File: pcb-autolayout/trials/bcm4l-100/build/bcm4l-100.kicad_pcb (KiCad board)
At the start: 4 copper layers, 80 x 60 mm, 120 parts, among them J1 MicroFit 2x4, J2 MicroFit 2x6, J3 SWD, Q1 SQD40P06 (P-MOS), Q11 AO3401A, Q12 MMBT3904, Q13 AO3401A, Q14 MMBT3904, Q15 AO3401A, Q16 MMBT3904, Q17 AO3401A, Q18 MMBT3904, SW1 RESET, U1 TPS54202, U2 AMS1117-3.3, U3 TJA1051T/3, U4 TJA1021T/20, U5 STM32F103C8T6, Y1 8MHz

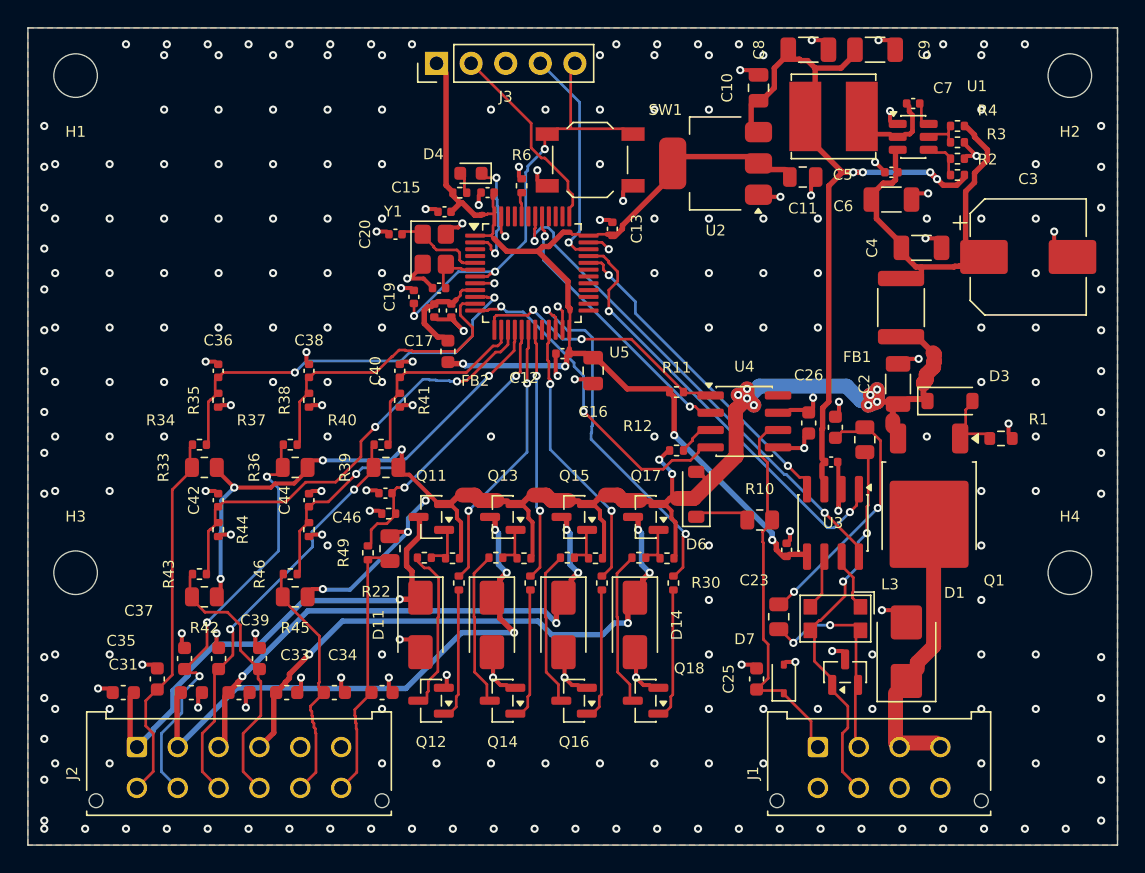
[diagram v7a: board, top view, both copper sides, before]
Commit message: 16/16 rule không chỉnh tay; placement repair; tất định KiCad 9 thật sự
- placer.repair_near: gỡ-đặt lại quanh chân đích, điểm từ điển (vượt C, vượt M)
- NEAR_REACH: linh kiện near vươn khỏi vùng khối tới quanh chân đích
- checks.near_gap: thước đo near dùng chung checker/placer
- kicad_board: canonicalize trước khi tô zone (KiCad 9 tô lệch µm theo thứ tự UUID);
  chuẩn hoá đa giác tô (bỏ đỉnh thẳng hàng, xoay, sắp)
- tests/test_placer.py; trial 16/16 KiCad 9 f116fcd59dba83db, KiCad 7 33b4f9200f4283d2

Co-Authored-By: Claude Opus 5.5 <noreply@anthropic.com>
Claude-Session: https://claude.ai/code/session_012jwodCpQFB8wopi3P3TnUz
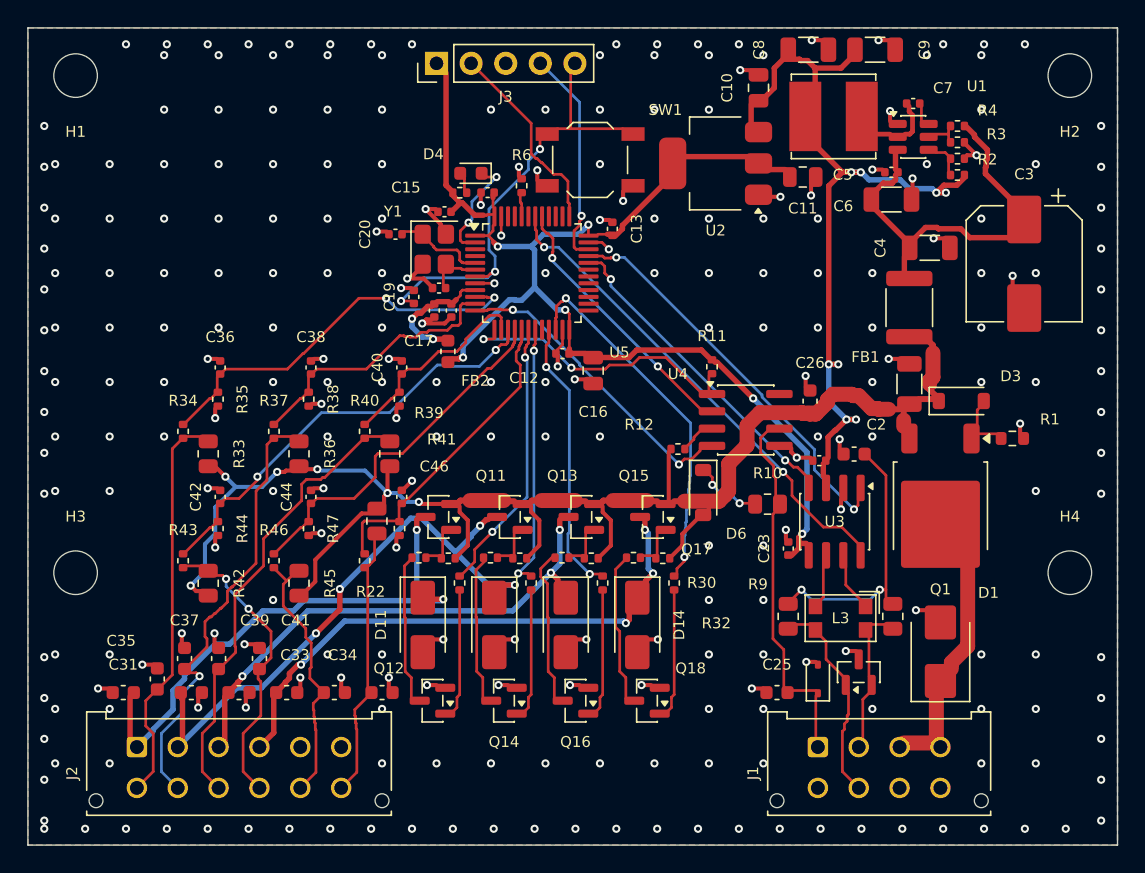
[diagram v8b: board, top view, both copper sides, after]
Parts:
- C20: renamed from C46; value 10n -> 20p
- C40: renamed from C20; value 20p -> 10n
- R11: renamed from R12; value 10k -> 4k7
- R12: renamed from R11; value 4k7 -> 10k
- moved R6 27.4 mm to (136.2, 71.6), turned to 90 degrees
- moved R24 27.4 mm to (136.1, 98.9), turned to 180 degrees
- moved C20 19.0 mm to (127.0, 75.2)
- moved R8 13.1 mm to (163.5, 103.2)
- moved R34 10.5 mm to (111.4, 89.6), turned to 90 degrees
- moved R37 10.5 mm to (118.1, 89.6), turned to 90 degrees
- moved C40 9.79 mm to (127.4, 84.9), turned to 90 degrees
- moved R50 9.42 mm to (127.3, 96.8)
- moved C46 9.26 mm to (127.4, 94.4)
- moved R40 8.92 mm to (124.7, 89.6)
- moved R43 8.61 mm to (111.4, 99.1), turned to 90 degrees
- moved R46 8.61 mm to (118.1, 99.1), turned to 90 degrees
- moved R49 8.61 mm to (124.7, 99.1), turned to 90 degrees
- moved R41 8.44 mm to (127.3, 87.3), turned to -90 degrees
- moved R39 6.96 mm to (126.6, 91.3), turned to 90 degrees
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- renumbered C40 to C46, R6 to R24, R43 to R34, R46 to R37, R48 to R39, R49 to R40, R50 to R41, R34 to R43, R37 to R46, R39 to R48, R40 to R49, R41 to R50, R24 to R6, R9 to R8, R8 to R9
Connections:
- C20 pad 1: IN6_M -> OSC_IN
- C40 pad 1: OSC_IN -> IN3_M
- C46 pad 1: IN3_M -> IN6_M
- R11 pad 1: LIN_WAKE -> LIN_RX
- R11 pad 2: VBAT_P -> +3V3
- R12 pad 1: LIN_RX -> LIN_WAKE
- R12 pad 2: +3V3 -> VBAT_P
- R24 pad 1: BOOT0 -> VBAT_P
- R24 pad 2: GND -> OUT2_G
- R34 pad 1: IN4 -> IN1
- R34 pad 2: IN4_M -> IN1_M
- R37 pad 1: IN5 -> IN2
- R37 pad 2: IN5_M -> IN2_M
- R39 pad 2: IN6 -> IN3
- R40 pad 1: IN6 -> IN3
- R40 pad 2: IN6_M -> IN3_M
- R41 pad 1: IN6_M -> IN3_M
- R43 pad 1: IN1 -> IN4
- R43 pad 2: IN1_M -> IN4_M
- R46 pad 1: IN2 -> IN5
- R46 pad 2: IN2_M -> IN5_M
- R48 pad 2: IN3 -> IN6
- R49 pad 1: IN3 -> IN6
- R49 pad 2: IN3_M -> IN6_M
- R50 pad 1: IN3_M -> IN6_M
- R6 pad 1: VBAT_P -> BOOT0
- R6 pad 2: OUT2_G -> GND
- R8 pad 1: CANL -> CANH
- R9 pad 1: CANH -> CANL
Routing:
- net VBAT_P: track 112.9 -> 99.6 mm, vias 18 -> 6
- net CANL: track 25.2 -> 12.1 mm, vias 2 -> 0
- net +3V3: track 74.3 -> 80.5 mm, vias 4 -> 6
- net CANH: track 12.7 -> 7.99 mm, vias 2 -> 0
- net GND: track 66.4 -> 62.3 mm, vias 258 -> 267
- net +5V: track 48.1 -> 52.1 mm, vias 4 -> 8
- net OUT1: track 33.6 -> 37.4 mm, vias 1 -> 2
- net OUT2: track 38.6 -> 42.0 mm, vias 3 -> 4
- net IN3: track 28.5 -> 31.5 mm, vias 2 -> 0
- net CAN_TX: track 30.9 -> 28.3 mm
- net IN5: track 15.4 -> 17.9 mm
- net LIN_RX: track 17.5 -> 20.0 mm
- net IN1: track 24.7 -> 27.2 mm
- net IN2_M: track 20.5 -> 18.1 mm
- net IN6_M: track 19.4 -> 21.4 mm, vias 2 -> 0
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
